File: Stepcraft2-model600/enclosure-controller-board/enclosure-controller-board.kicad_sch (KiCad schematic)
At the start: 15 parts, among them J1 Screw_Terminal_01x06, J2 Screw_Terminal_01x06, J3 Screw_Terminal_01x02, T1 BC547B, T2 BC547B, U1 MCT6, X1 DA15_Plug_MountingHoles, X11 DA15_Receptacle_MountingHoles

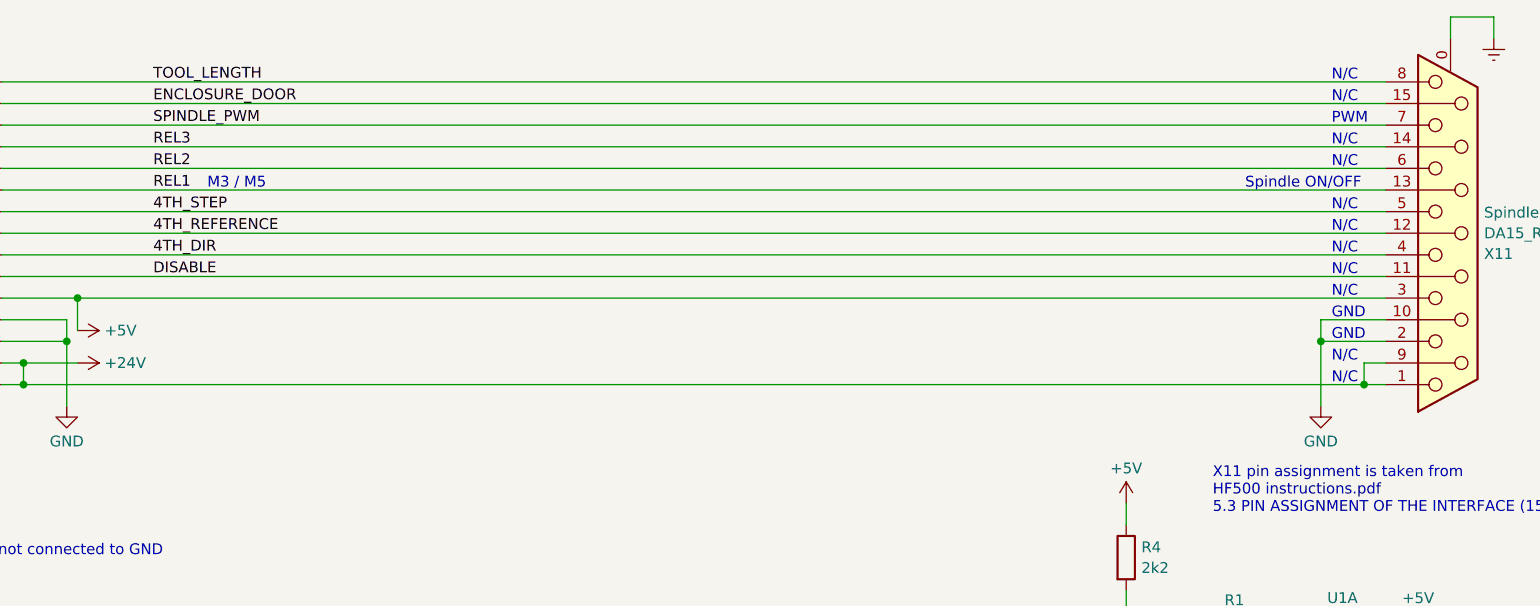
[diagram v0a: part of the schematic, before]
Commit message: Add note about SPINDLE_SPEED signal on Stepcraft
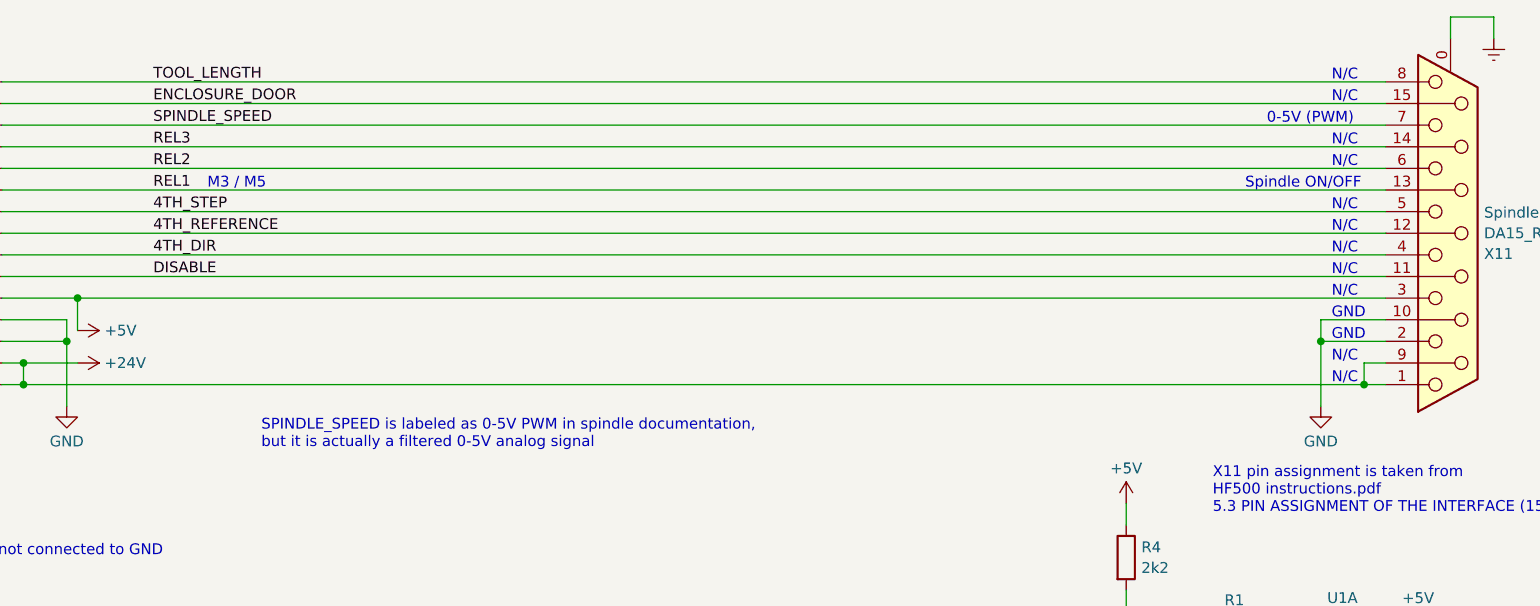
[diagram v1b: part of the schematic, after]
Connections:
- net SPINDLE_PWM renamed SPINDLE_SPEED
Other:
- note added: "0-5V (PWM)"
- note added: "SPINDLE_SPEED is labeled as 0-5V PWM in spindle documentation, but it is actually a filtered 0-5V analog signal"
- note removed: "PWM"
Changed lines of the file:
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@@
     (effects (font (size 1.27 1.27)) (justify left bottom))
   )
-  (text "PWM" (at 227.33 25.4 0)
+  (text "0-5V (PWM)" (at 219.71 25.4 0)
+    (effects (font (size 1.27 1.27)) (justify left bottom))
+  )
+  (text "SPINDLE_SPEED is labeled as 0-5V PWM in spindle documentation,\nbut it is actually a filtered 0-5V analog signal"
+    (at 101.6 63.5 0)
     (effects (font (size 1.27 1.27)) (justify left bottom))
   )
@@
     (effects (font (size 1.27 1.27)) (justify left bottom))
   )
-  (label "SPINDLE_PWM" (at 88.9 25.4 0) (fields_autoplaced)
+  (label "SPINDLE_SPEED" (at 88.9 25.4 0) (fields_autoplaced)
     (effects (font (size 1.27 1.27)) (justify left bottom))
   )

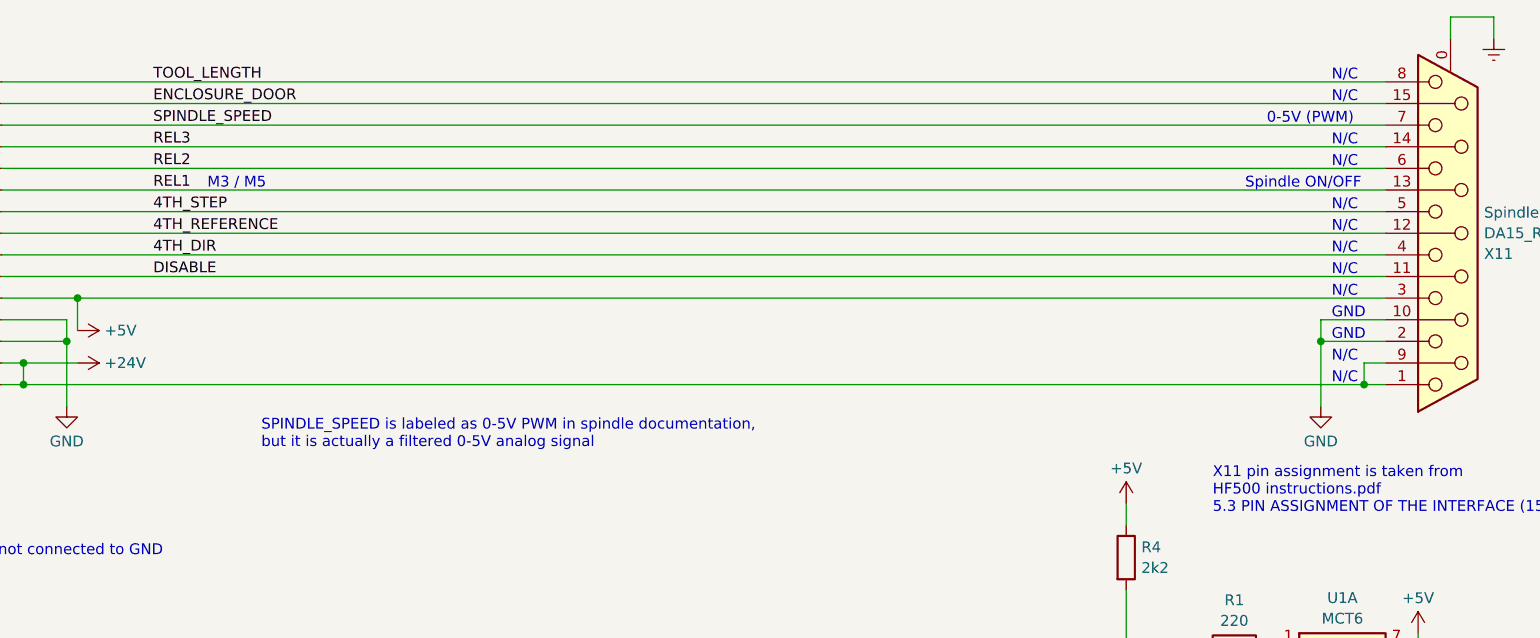
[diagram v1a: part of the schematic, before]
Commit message: Fix Stepcraft spindle PWM documentation
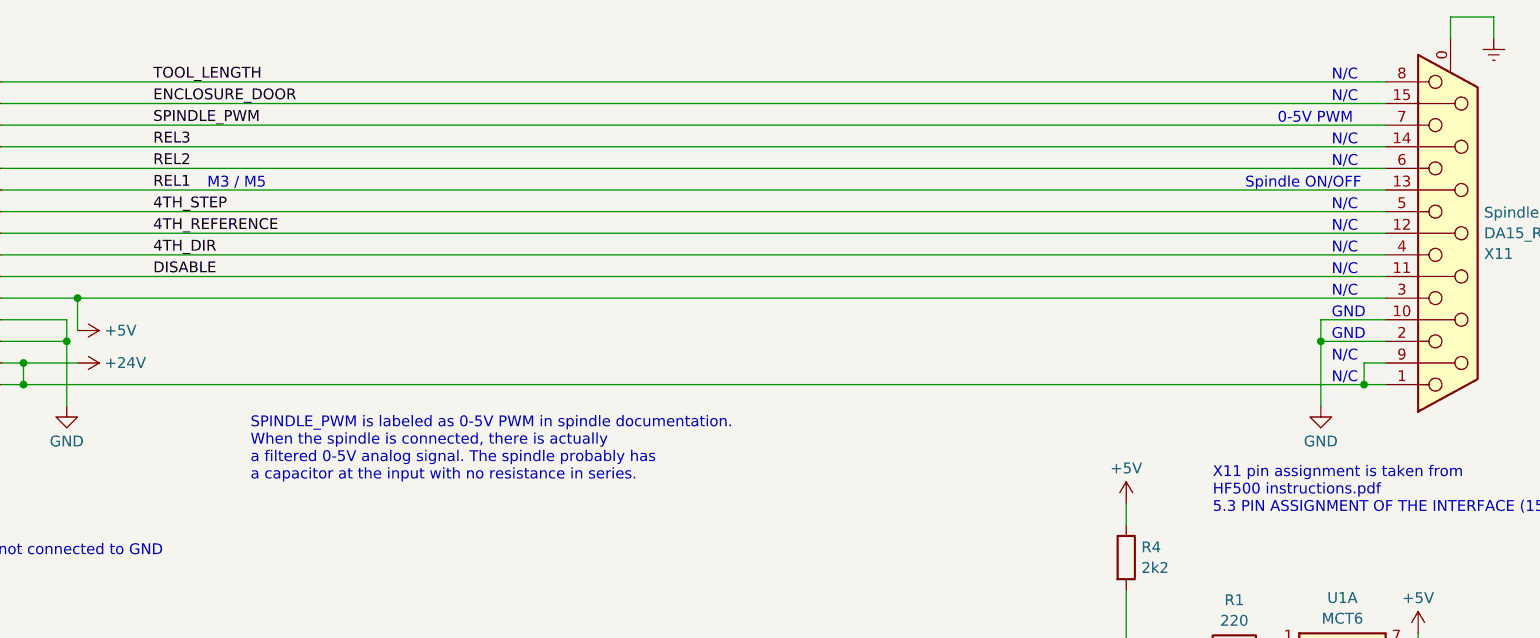
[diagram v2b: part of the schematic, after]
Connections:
- net SPINDLE_SPEED renamed SPINDLE_PWM
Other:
- note added: "0-5V PWM"
- note added: "SPINDLE_PWM is labeled as 0-5V PWM in spindle documentation. When the spindle is connected, there is actually a filtered 0-5V analog signal. The spindle probably has a capacitor at the input with no resistance in series."
- note removed: "0-5V (PWM)"
- note removed: "SPINDLE_SPEED is labeled as 0-5V PWM in spindle documentation, but it is actually a filtered 0-5V analog signal"
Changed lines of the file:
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@@
     (effects (font (size 1.27 1.27)) (justify left bottom))
   )
-  (text "0-5V (PWM)" (at 219.71 25.4 0)
+  (text "0-5V PWM" (at 220.98 25.4 0)
     (effects (font (size 1.27 1.27)) (justify left bottom))
   )
-  (text "SPINDLE_SPEED is labeled as 0-5V PWM in spindle documentation,\nbut it is actually a filtered 0-5V analog signal"
-    (at 101.6 63.5 0)
+  (text "SPINDLE_PWM is labeled as 0-5V PWM in spindle documentation.\nWhen the spindle is connected, there is actually\na filtered 0-5V analog signal. The spindle probably has\na capacitor at the input with no resistance in series."
+    (at 100.33 67.31 0)
     (effects (font (size 1.27 1.27)) (justify left bottom))
   )
@@
     (effects (font (size 1.27 1.27)) (justify left bottom))
   )
-  (label "SPINDLE_SPEED" (at 88.9 25.4 0) (fields_autoplaced)
+  (label "SPINDLE_PWM" (at 88.9 25.4 0) (fields_autoplaced)
     (effects (font (size 1.27 1.27)) (justify left bottom))
   )
